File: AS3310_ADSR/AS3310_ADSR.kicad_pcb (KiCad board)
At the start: 2 copper layers, 71.1 x 20.3 mm, 26 parts, among them J1 ADSR_Pots, J2 Gate, J3 Peak, J4 AtkOut, J5 EnvOut, J6 Trigger, J7 Power, U1 AS3310, U2 TL071

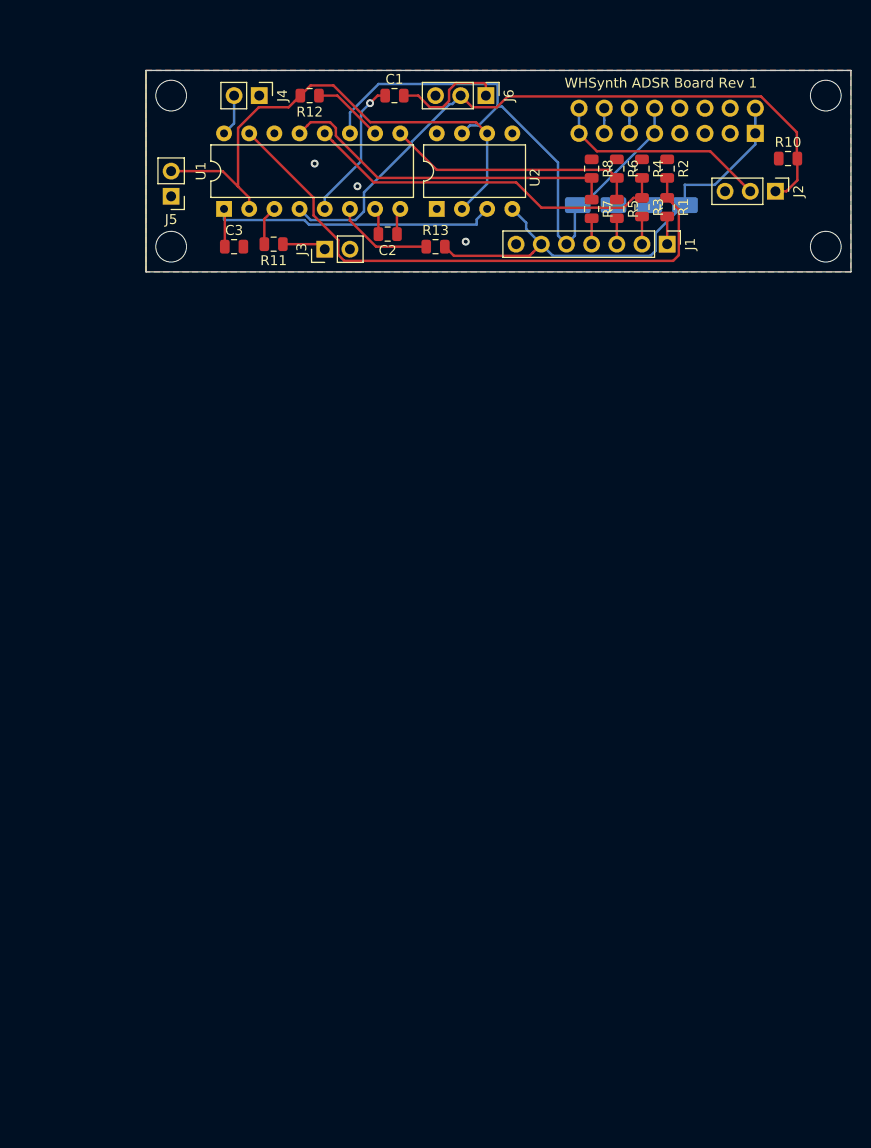
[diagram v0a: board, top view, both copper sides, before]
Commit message: Combine IO and main ADSR boards
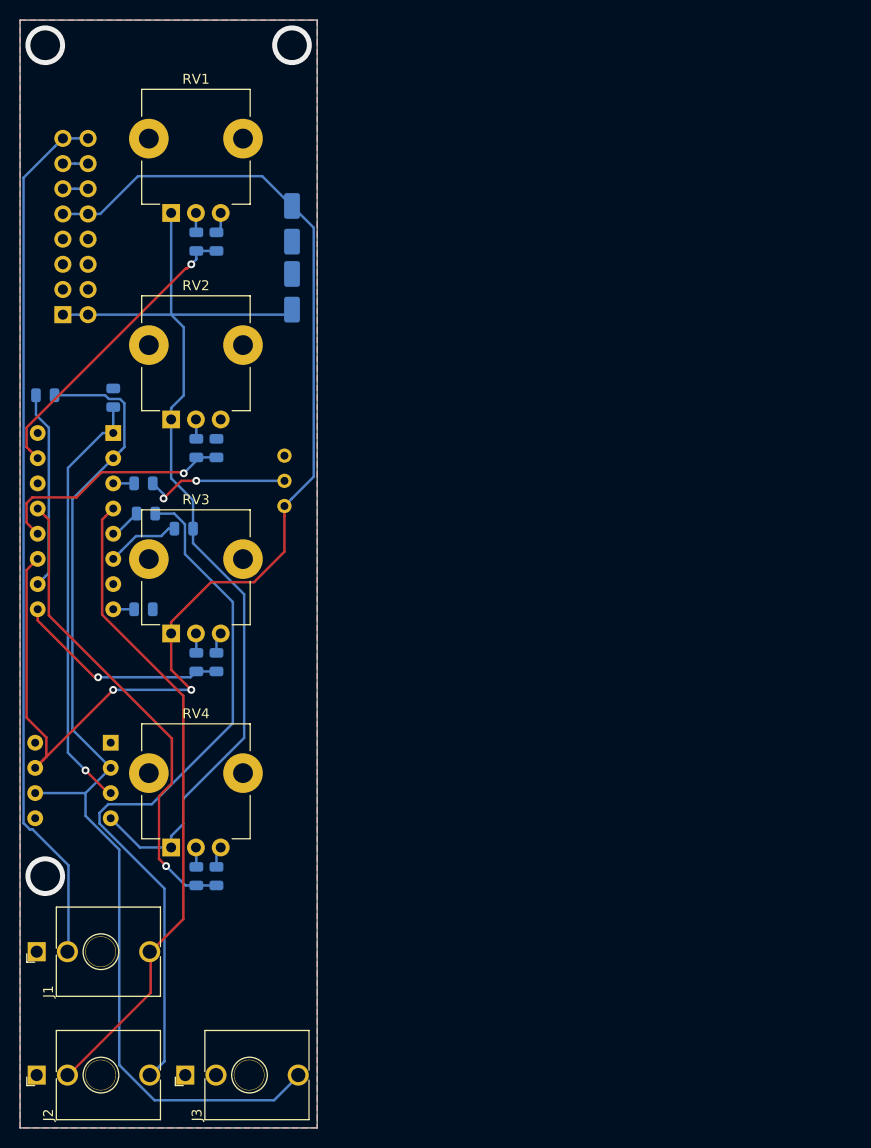
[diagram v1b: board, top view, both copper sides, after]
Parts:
- removed J5: EnvOut, Connector_PinHeader_2.54mm:PinHeader_1x02_P2.54mm_Vertical
- removed J6: Trigger, Connector_PinHeader_2.54mm:PinHeader_1x03_P2.54mm_Vertical
- removed J7: Power, Connector_IDC:IDC-Header_2x08_P2.54mm_Vertical
- removed R12: 30K, Resistor_SMD:R_0805_2012Metric
- removed R13: 470, Resistor_SMD:R_0805_2012Metric
- added R9: 30K, Resistor_SMD:R_0805_2012Metric, B.Cu at (66.0, 86.1)
- added RV1: 100K, Eurorack:Potentiometer_TT_P0915N, F.Cu at (81.3, 60.2)
- added RV2: 100K, Eurorack:Potentiometer_TT_P0915N, F.Cu at (81.3, 81.0)
- added RV3: 100K, Eurorack:Potentiometer_TT_P0915N, F.Cu at (81.3, 102.6)
- added RV4: R_POT_US, Eurorack:Potentiometer_TT_P0915N, F.Cu at (81.3, 124.2)
- added RV5: 100K, Potentiometer_THT:Potentiometer_Bourns_3296W_Vertical, B.Cu at (90.2, 97.3)
- C1, C2, C3, R1, R10, R2, R3, R4, R7, R8, U1, U2: moved to B.Cu
- C4, C5: value 10uF -> CP1
- J1: value ADSR_Pots -> Gate; footprint Connector_PinHeader_2.54mm:PinHeader_1x07_P2.54mm_Vertical -> Eurorack:Jack_3.5mm_QingPu_WQP-PJ398SM_Vertical_CircularHoles
- J2: value Gate -> Trigger; footprint Connector_PinHeader_2.54mm:PinHeader_1x03_P2.54mm_Vertical -> Eurorack:Jack_3.5mm_QingPu_WQP-PJ398SM_Vertical_CircularHoles
- J3: value Peak -> Env; footprint Connector_PinHeader_2.54mm:PinHeader_1x02_P2.54mm_Vertical -> Eurorack:Jack_3.5mm_QingPu_WQP-PJ398SM_Vertical_CircularHoles
- J4: value AtkOut -> Conn_01x16; footprint Connector_PinHeader_2.54mm:PinHeader_1x02_P2.54mm_Vertical -> Connector_IDC:IDC-Header_2x08_P2.54mm_Vertical; moved to B.Cu
- R11: value 10K -> 470; moved to B.Cu
- R5: value 22K -> R_US; moved to B.Cu
- R6: value 16K -> R_US; moved to B.Cu
- moved J2 112.2 mm to (71.6, 154.7), turned to 90 degrees
- moved J1 91.4 mm to (71.6, 142.2), turned to 90 degrees
- moved J3 83.7 mm to (86.6, 154.7)
- moved R8 80.8 mm to (83.3, 134.6), turned to 90 degrees
- moved R7 78.2 mm to (81.3, 134.6)
- moved R10 72.8 mm to (75.9, 95.0)
- moved R6 64.1 mm to (83.3, 113.0), turned to 90 degrees
- moved U2 63.1 mm to (72.6, 121.2), turned to 180 degrees
- moved R5 62.4 mm to (81.3, 113.0)
- moved R4 51.4 mm to (83.3, 91.4), turned to 90 degrees
- moved R3 51.1 mm to (81.3, 91.4)
- moved C1 49.1 mm to (76.2, 98.0)
- moved R1 47.6 mm to (81.3, 70.6)
- moved R2 46.1 mm to (83.3, 70.6), turned to 90 degrees
- moved C2 45.2 mm to (75.9, 107.7), turned to 0 degrees
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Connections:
- C1 pad 2: Net-(C1-Pad2) -> /Trigger
- J4 pad 1: GNDREF -> -12V
- J4 pad 2: Net-(J4-Pad2) -> -12V
- R1 pad 1: /Attack -> Net-(R1-Pad1)
- R1 pad 2: Net-(J1-Pad1) -> /Attack
- R10 pad 1: GNDREF -> Net-(R10-Pad1)
- R10 pad 2: Net-(J2-Pad1) -> Net-(R10-Pad2)
- R11 pad 1: Net-(J3-Pad1) -> Net-(R11-Pad1)
- R11 pad 2: Net-(R11-Pad2) -> -12V
- R2 pad 1: GNDREF -> /Attack
- R2 pad 2: /Attack -> GNDREF
- R3 pad 1: /Decay -> Net-(R3-Pad1)
- R3 pad 2: Net-(J1-Pad2) -> /Decay
- R4 pad 1: GNDREF -> /Decay
- R4 pad 2: /Decay -> GNDREF
- R5 pad 1: /Sustain -> Net-(R5-Pad1)
- R5 pad 2: Net-(J1-Pad3) -> /Sustain
- R6 pad 1: GNDREF -> /Sustain
- R6 pad 2: /Sustain -> GNDREF
- R7 pad 1: /Release -> Net-(R7-Pad1)
- R7 pad 2: Net-(J1-Pad4) -> /Release
- R8 pad 1: GNDREF -> /Release
- R8 pad 2: /Release -> GNDREF
- U1 pad 16: Net-(J4-Pad2) -> Net-(U1-Pad16)
- U1 pad 2: Net-(J5-Pad2) -> Net-(J3-PadT)
- U1 pad 3: Net-(R11-Pad2) -> Net-(R10-Pad1)
- U1 pad 4: Net-(J2-Pad1) -> /Gate
- U1 pad 6: Net-(R13-Pad1) -> Net-(R11-Pad1)
- U2 pad 2: Net-(J5-Pad2) -> Net-(J3-PadT)
- U2 pad 6: Net-(J5-Pad2) -> Net-(J3-PadT)
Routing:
- net Net-(J3-PadT): track 0.00 -> 106.6 mm
- net /Rear_Gate: track 0.00 -> 88.3 mm
- net /Trigger: track 0.00 -> 72.4 mm
- net Net-(J2-Pad1): track 67.1 -> 0.00 mm
- net +12V: track 60.3 -> 126.8 mm, vias 0 -> 2
- net -12V: track 48.2 -> 101.8 mm
- net Net-(J5-Pad2): track 53.6 -> 0.00 mm
- net /Gate: track 22.3 -> 65.8 mm
- net /Attack: track 59.1 -> 30.6 mm, vias 0 -> 1
- net Net-(R10-Pad2): track 0.00 -> 14.9 mm, vias 0 -> 2
- net /Release: track 34.9 -> 48.4 mm, vias 0 -> 1
- net Net-(R9-Pad1): track 7.24 -> 20.1 mm
- net /Decay: track 37.5 -> 24.9 mm, vias 0 -> 1
- net Net-(C1-Pad2): track 11.6 -> 0.00 mm
- net Net-(C1-Pad1): track 14.4 -> 3.21 mm, vias 1 -> 0
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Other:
- board size 71.1 x 20.3 mm -> 30 x 111.8 mm
- board text removed: "WHSynth ADSR Board Rev 1"
